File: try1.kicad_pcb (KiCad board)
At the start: 2 copper layers, 168.9 x 102 mm, 33 parts, among them J10 Archon-connector-modules-Driv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, J11 Archon-connector-modules-Driv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, J2 Archon-connector-modules-Heat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, J21 DB37, J22 DB37, J3 Archon-connector-modules-Driv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, J31 DB9, J4 Archon-connector-modules-LVBi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, J41 CONN_DVI, J5 Archon-connector-modules-ADC, J6 Archon-connector-modules-ADC, J7 Archon-connector-modules-ADC, J8 Archon-connector-modules-ADC, J9 Archon-connector-modules-HVBi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, P1 CONN_02X02

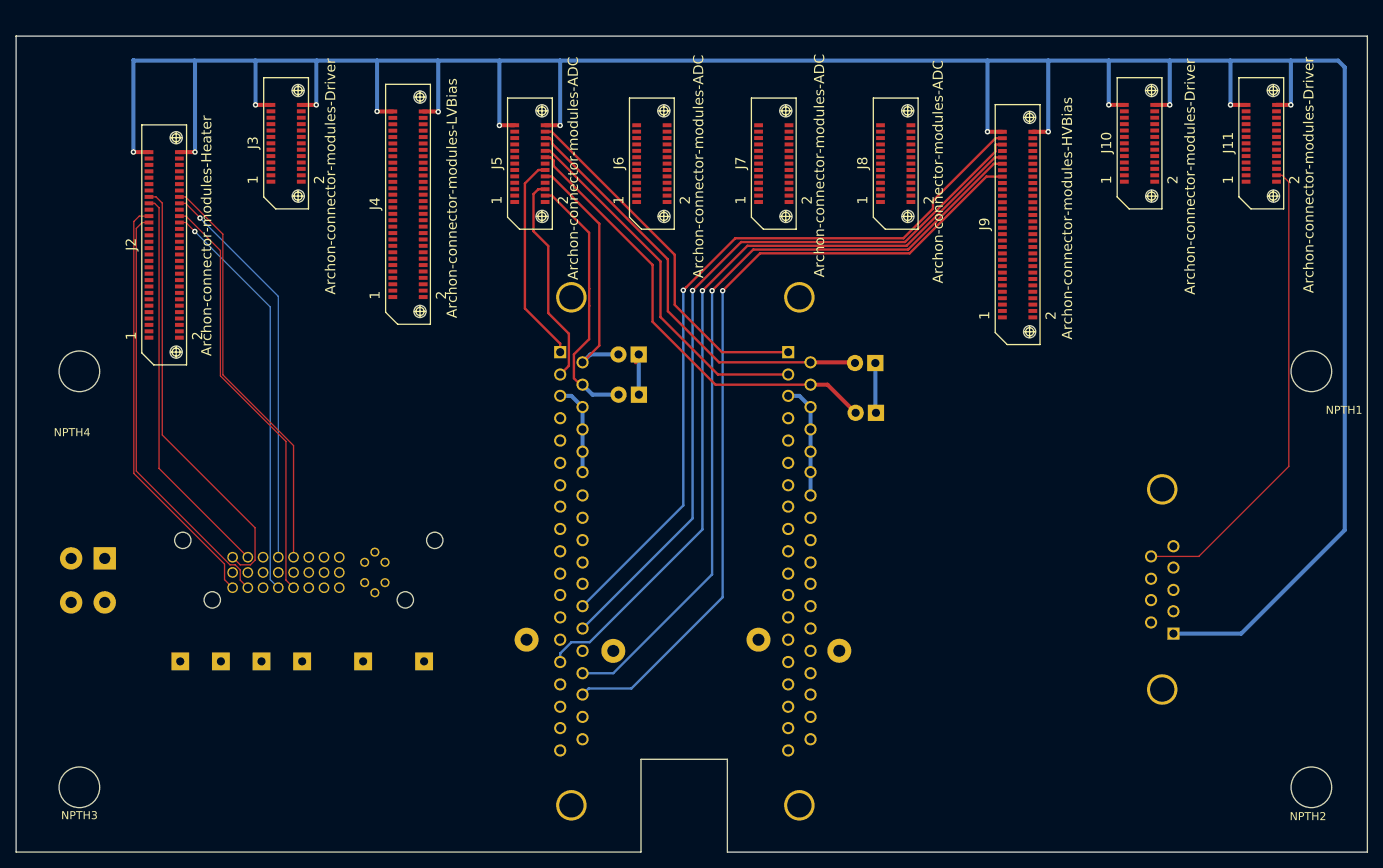
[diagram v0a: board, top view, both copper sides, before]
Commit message: WIP Retrace Everything
I think this is working.  I still have to adjust everything, but
these connections are the rough paths I want.
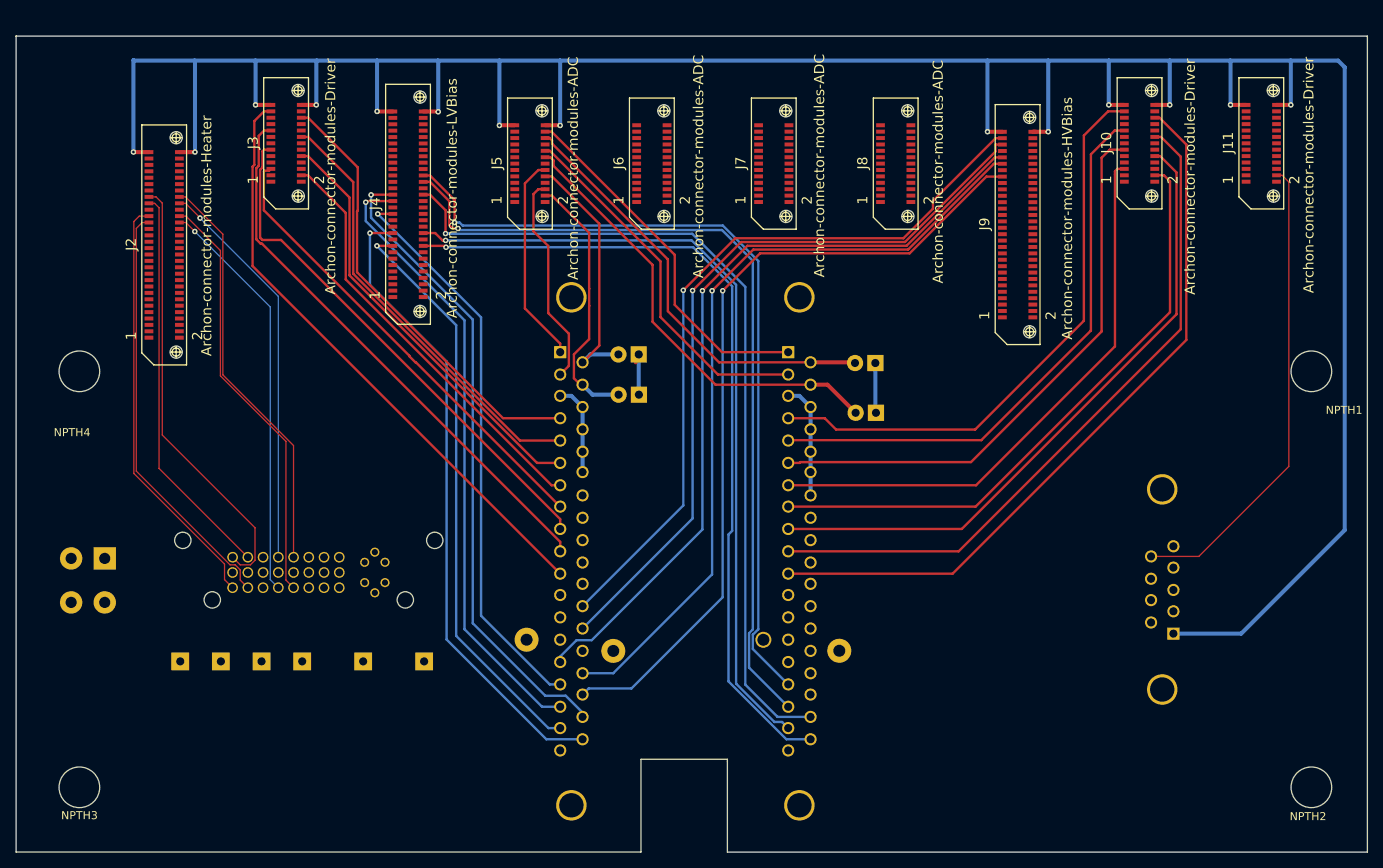
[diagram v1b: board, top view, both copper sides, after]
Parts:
- moved W1 0.61 mm to (139.5, 98.6)
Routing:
- net /ResetLO_R: track 0.00 -> 106.3 mm, vias 0 -> 1
- net /GainSW2_R: track 0.00 -> 105.0 mm, vias 0 -> 1
- net /-15V_R: track 0.01 -> 103.6 mm, vias 0 -> 1
- net /VLg_R: track 0.00 -> 103.0 mm, vias 0 -> 1
- net /+15V_R: track 0.00 -> 100.5 mm, vias 0 -> 1
- net /TGX: track 0.00 -> 91.6 mm
- net /P3X: track 0.41 -> 86.8 mm
- net /P2X: track 0.41 -> 81.4 mm
- net /ResetLO_L: track 0.00 -> 80.4 mm, vias 0 -> 1
- net /-15V_L: track 0.00 -> 79.8 mm, vias 0 -> 1
- net /GainSW2_L: track 0.00 -> 77.9 mm, vias 0 -> 1
- net /P1X: track 0.01 -> 76.4 mm
- net /P1Y: track 0.00 -> 75.2 mm
- net /S3X: track 0.00 -> 72.6 mm
- net /+15V_L: track 0.00 -> 72.6 mm, vias 0 -> 1
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
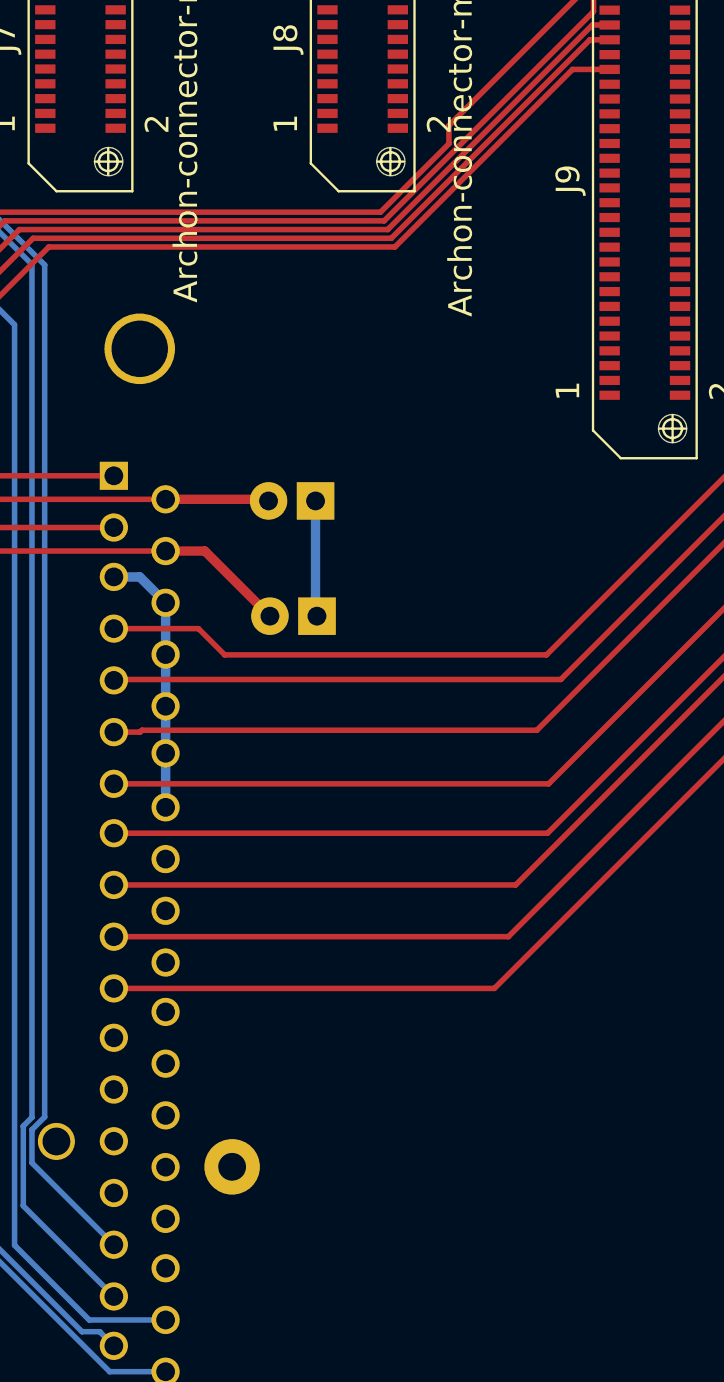
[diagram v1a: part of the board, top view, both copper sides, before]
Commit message: WIP Add Some HV Traces
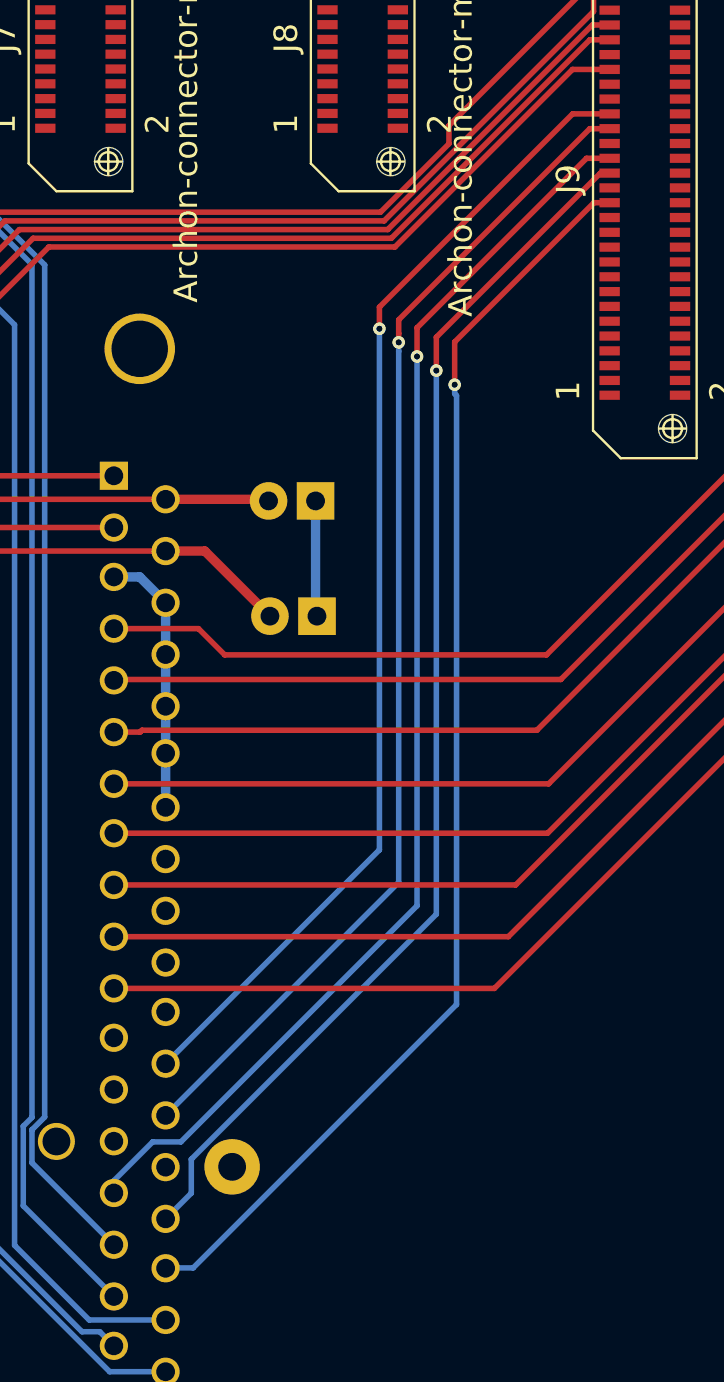
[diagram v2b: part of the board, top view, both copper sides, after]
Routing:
- net /VRD1_R: track 0.00 -> 68.9 mm, vias 0 -> 1
- net /VRD2_R: track 0.04 -> 68.6 mm, vias 0 -> 1
- net /VDD_C: track 0.00 -> 66.7 mm, vias 0 -> 1
- net /VDD_A: track 0.00 -> 63.9 mm, vias 0 -> 1
- net /ResetHI_R: track 0.00 -> 62.4 mm, vias 0 -> 1
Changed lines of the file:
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@@
     (links 112)
     (no_connects 40)
-    (area 46.077299 23.087299 215.012701 125.112701)
+    (area 28.76 13.19 240.694286 138.820001)
     (thickness 1.6)
     (drawings 37)
-    (tracks 486)
+    (tracks 527)
     (zones 0)
     (modules 33)
@@
     (aux_axis_origin 0 0)
     (grid_origin 52.17 35.59)
-    (visible_elements 7FFFF7FF)
+    (visible_elements 7FFFFFFF)
     (pcbplotparams
       (layerselection 0x00030_80000001)
@@
   (segment (start 77.94008 32.50204) (end 77.09017 32.50204) (width 0.3) (layer F.Cu) (net 311) (status 10))
   (segment (start 77.09017 32.50204) (end 75.86998 33.72223) (width 0.3) (layer F.Cu) (net 311))
-  (segment (start 184.62008 32.50204) (end 182.58796 32.50204) (width 0.3) (layer F.Cu) (net 312) (status 400000))
-  (segment (start 147.173 70.863) (end 142.603 70.863) (width 0.3) (layer F.Cu) (net 312) (status 800000))
+  (segment (start 184.62008 32.50204) (end 182.58796 32.50204) (width 0.3) (layer F.Cu) (net 312))
+  (segment (start 147.173 70.863) (end 142.603 70.863) (width 0.3) (layer F.Cu) (net 312))
   (segment (start 148.59 72.28) (end 147.173 70.863) (width 0.3) (layer F.Cu) (net 312))
   (segment (start 165.97 72.28) (end 148.59 72.28) (width 0.3) (layer F.Cu) (net 312))
@@
   (segment (start 179.56 35.53) (end 179.56 58.69) (width 0.3) (layer F.Cu) (net 312))
   (segment (start 182.58796 32.50204) (end 179.56 35.53) (width 0.3) (layer F.Cu) (net 312))
-  (segment (start 184.62008 34.90234) (end 183.41766 34.90234) (width 0.3) (layer F.Cu) (net 313) (status 400000))
-  (segment (start 166.74 73.61) (end 142.65 73.61) (width 0.3) (layer F.Cu) (net 313) (status 800000))
+  (segment (start 184.62008 34.90234) (end 183.41766 34.90234) (width 0.3) (layer F.Cu) (net 313))
+  (segment (start 166.74 73.61) (end 142.65 73.61) (width 0.3) (layer F.Cu) (net 313))
   (segment (start 180.44 59.91) (end 166.74 73.61) (width 0.3) (layer F.Cu) (net 313))
   (segment (start 180.44 37.88) (end 180.44 59.91) (width 0.3) (layer F.Cu) (net 313))
   (segment (start 183.41766 34.90234) (end 180.44 37.88) (width 0.3) (layer F.Cu) (net 313))
-  (segment (start 142.65 73.61) (end 142.603 73.657) (width 0.3) (layer F.Cu) (net 313) (status C00000))
-  (segment (start 142.603 76.451) (end 144.019 76.451) (width 0.3) (layer F.Cu) (net 314) (status 400000))
-  (segment (start 182.79244 37.29756) (end 184.62008 37.29756) (width 0.3) (layer F.Cu) (net 314) (status 800000))
+  (segment (start 142.65 73.61) (end 142.603 73.657) (width 0.3) (layer F.Cu) (net 313))
+  (segment (start 142.603 76.451) (end 144.019 76.451) (width 0.3) (layer F.Cu) (net 314))
+  (segment (start 182.79244 37.29756) (end 184.62008 37.29756) (width 0.3) (layer F.Cu) (net 314))
   (segment (start 181.78 38.31) (end 182.79244 37.29756) (width 0.3) (layer F.Cu) (net 314))
   (segment (start 181.78 60.02) (end 181.78 38.31) (width 0.3) (layer F.Cu) (net 314))
@@
   (via (at 129.49 54.87) (size 0.6858) (drill 0.3302) (layers F.Cu B.Cu) (net 373))
   (segment (start 169.38008 35.86246) (end 168.88694 35.86246) (width 0.1524) (layer F.Cu) (net 373) (status 30))
+  (segment (start 161.009 57.688) (end 161.009 58.172933) (width 0.3) (layer B.Cu) (net 374))
+  (segment (start 161.009 58.172933) (end 161.1106 58.274533) (width 0.3) (layer B.Cu) (net 374))
+  (segment (start 161.1106 58.274533) (end 161.1106 91.1652) (width 0.3) (layer B.Cu) (net 374))
+  (segment (start 161.1106 91.1652) (end 146.8866 105.3892) (width 0.3) (layer B.Cu) (net 374))
+  (segment (start 146.8866 105.3892) (end 145.4148 105.3892) (width 0.3) (layer B.Cu) (net 374))
+  (segment (start 145.4148 105.3892) (end 145.397 105.407) (width 0.3) (layer B.Cu) (net 374))
+  (segment (start 169.38008 47.85888) (end 168.53017 47.85888) (width 0.3) (layer F.Cu) (net 374))
+  (segment (start 168.53017 47.85888) (end 161.009 55.38005) (width 0.3) (layer F.Cu) (net 374))
+  (segment (start 161.009 55.38005) (end 161.009 57.688) (width 0.3) (layer F.Cu) (net 374))
+  (via (at 161.009 57.688) (size 0.6858) (drill 0.3302) (layers F.Cu B.Cu) (net 374))
+  (segment (start 145.397 102.74) (end 146.785 101.352) (width 0.3) (layer B.Cu) (net 375))
+  (segment (start 146.785 101.352) (end 146.785 99.5218) (width 0.3) (layer B.Cu) (net 375))
+  (segment (start 146.785 99.5218) (end 160.0184 86.2884) (width 0.3) (layer B.Cu) (net 375))
+  (segment (start 160.0184 86.2884) (end 160.0184 56.926) (width 0.3) (layer B.Cu) (net 375))
+  (segment (start 160.0184 56.926) (end 160.0184 55.1226) (width 0.3) (layer F.Cu) (net 375))
+  (segment (start 160.0184 55.1226) (end 168.87978 46.26122) (width 0.3) (layer F.Cu) (net 375))
+  (segment (start 168.87978 46.26122) (end 169.38008 46.26122) (width 0.3) (layer F.Cu) (net 375))
+  (via (at 160.0184 56.926) (size 0.6858) (drill 0.3302) (layers F.Cu B.Cu) (net 375))
+  (segment (start 158.977 56.164) (end 158.977 85.8312) (width 0.3) (layer B.Cu) (net 376))
+  (segment (start 158.977 85.8312) (end 146.2262 98.582) (width 0.3) (layer B.Cu) (net 376))
+  (segment (start 146.2262 98.582) (end 144.7022 98.582) (width 0.3) (layer B.Cu) (net 376))
+  (segment (start 144.7022 98.582) (end 142.603 100.6812) (width 0.3) (layer B.Cu) (net 376))
+  (segment (start 142.603 100.6812) (end 142.603 101.343) (width 0.3) (layer B.Cu) (net 376))
+  (segment (start 169.38008 45.46112) (end 168.13048 45.46112) (width 0.3) (layer F.Cu) (net 376))
+  (segment (start 168.13048 45.46112) (end 158.977 54.6146) (width 0.3) (layer F.Cu) (net 376))
+  (segment (start 158.977 54.6146) (end 158.977 56.164) (width 0.3) (layer F.Cu) (net 376))
+  (via (at 158.977 56.164) (size 0.6858) (drill 0.3302) (layers F.Cu B.Cu) (net 376))
   (segment (start 143.0598 100.9802) (end 143.0344 101.0056) (width 0.1524) (layer F.Cu) (net 376) (status 30))
+  (segment (start 169.38008 43.86092) (end 168.30828 43.86092) (width 0.3) (layer F.Cu) (net 378))
+  (segment (start 168.30828 43.86092) (end 157.9864 54.1828) (width 0.3) (layer F.Cu) (net 378))
+  (segment (start 157.9864 54.1828) (end 157.9864 54.917061) (width 0.3) (layer F.Cu) (net 378))
+  (segment (start 157.9864 54.917061) (end 157.9864 55.401994) (width 0.3) (layer F.Cu) (net 378))
+  (segment (start 157.9864 55.886927) (end 157.9864 55.401994) (width 0.3) (layer B.Cu) (net 378))
+  (segment (start 157.9864 84.5626) (end 157.9864 55.886927) (width 0.3) (layer B.Cu) (net 378))
+  (segment (start 145.397 97.152) (end 157.9864 84.5626) (width 0.3) (layer B.Cu) (net 378))
+  (via (at 157.9864 55.401994) (size 0.6858) (drill 0.3302) (layers F.Cu B.Cu) (net 378))
+  (segment (start 169.38008 43.06082) (end 167.38118 43.06082) (width 0.3) (layer F.Cu) (net 379))
+  (segment (start 167.38118 43.06082) (end 156.945 53.497) (width 0.3) (layer F.Cu) (net 379))
+  (segment (start 156.945 53.497) (end 156.945 54.6654) (width 0.3) (layer F.Cu) (net 379))
+  (segment (start 156.945 54.6654) (end 156.945 82.81) (width 0.3) (layer B.Cu) (net 379))
+  (segment (start 156.945 82.81) (end 145.397 94.358) (width 0.3) (layer B.Cu) (net 379))
+  (via (at 156.945 54.6654) (size 0.6858) (drill 0.3302) (layers F.Cu B.Cu) (net 379))
 )
